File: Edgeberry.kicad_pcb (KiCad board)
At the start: 2 copper layers, 135 x 90 mm, 171 parts, among them J1 Molex_KK_1x02_P2.54mm_CONN, P1 Barrel_Jack_CONN, Q1 BC547, Q2 BC547, Q3 BC547, SW1 SW_PUSH, U1 24LC256, U2 LM2596S-5.0

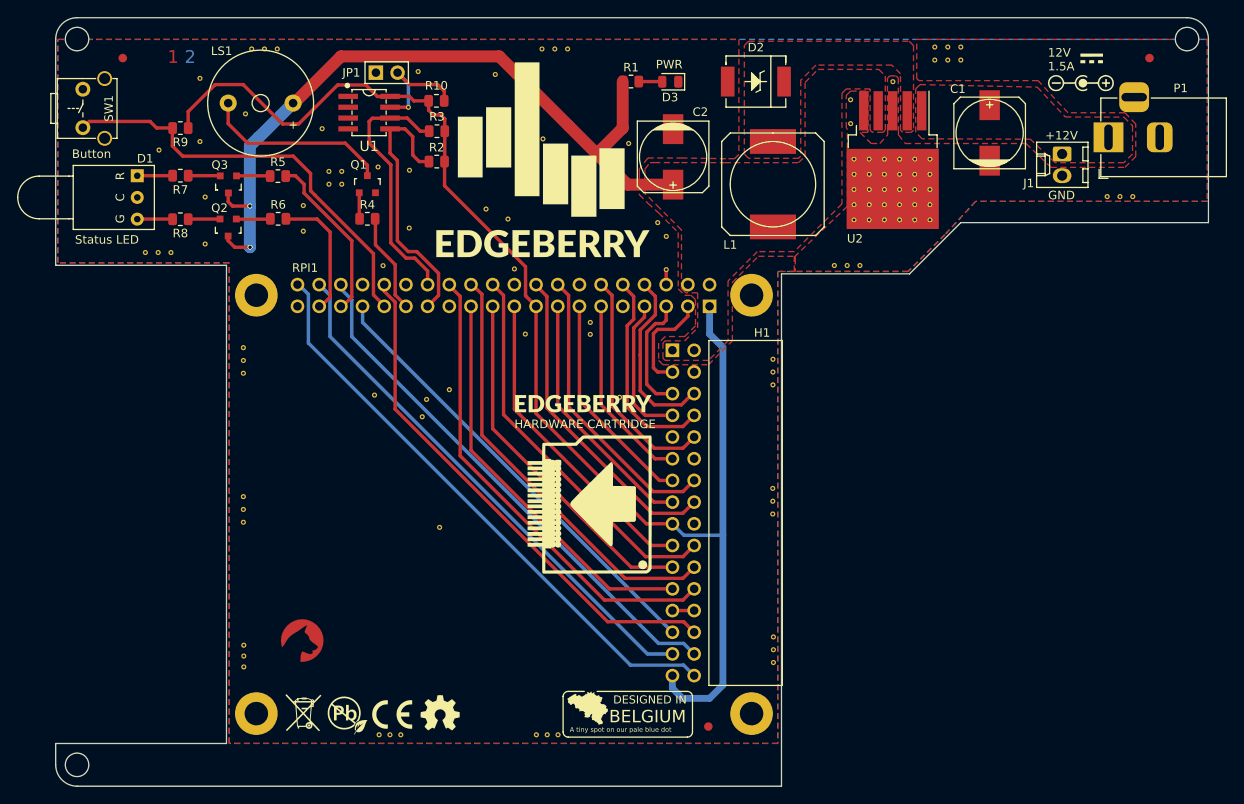
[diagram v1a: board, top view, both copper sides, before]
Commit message: Board:  improvements for fabrications
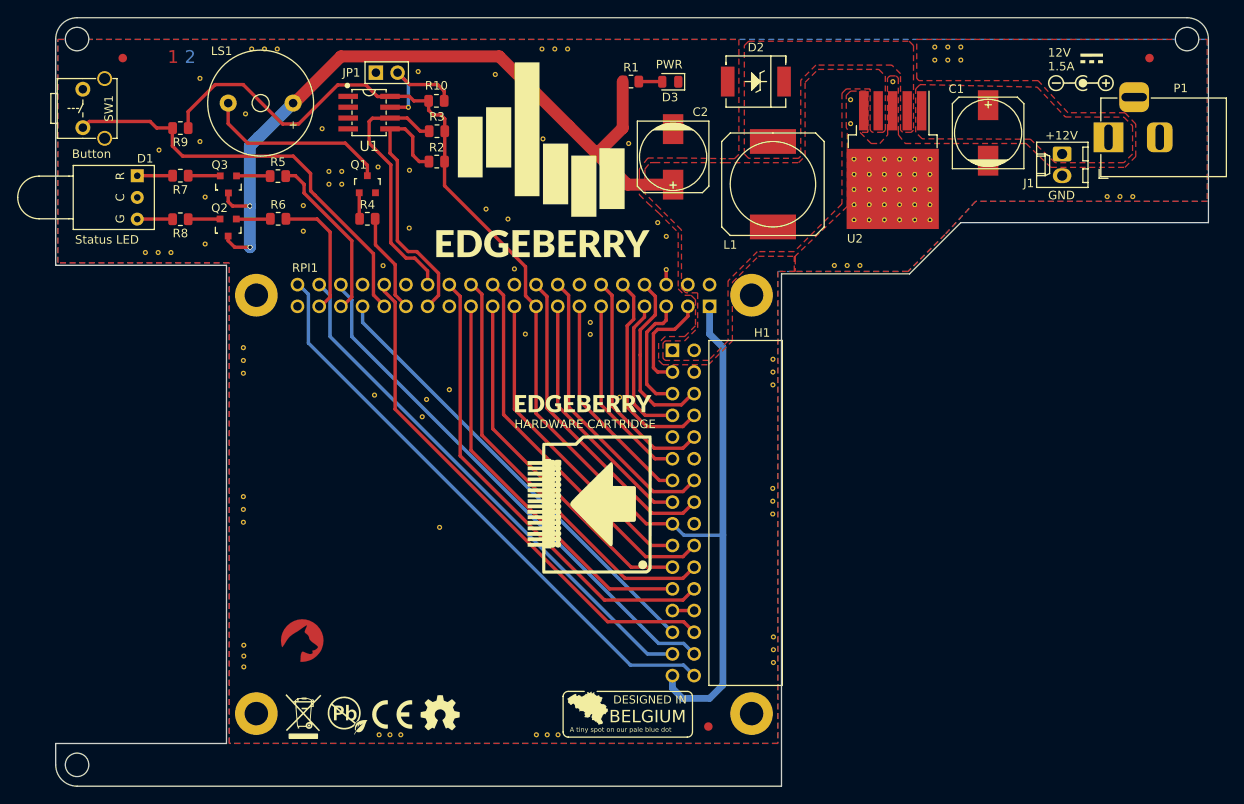
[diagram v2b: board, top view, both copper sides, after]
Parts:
- H1: value 2X16Pin_2.54mm_Right_Angle_Receptacle_Connector -> 2X16Pin_P2.54mm_Horizontal_Receptacle_Connector
- RPI1: value 2X20Pin_2.54mm_Receptacle_Connector -> 2X20Pin_2.54mm_Receptacle_CONN
- SW1: value SW_PUSH -> SW_PUSH_Horizontal
- moved C1 0.18 mm to (192.8, 65.3)
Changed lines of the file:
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@@
   (net 43 "Net-(Q3-Pad2)")
   (footprint "Capacitors_SMD:c_elec_8x10" (layer "F.Cu")
-    (at 193.028 65.2672 90)
+    (at 192.849 65.2672 90)
     (descr "SMT capacitor, aluminium electrolytic, 8x10")
     (property "Sheetfile" "Edgeberry.kicad_sch")
@@
       (effects (font (size 1 1) (thickness 0.15)))
     )
-    (fp_text value "SW_PUSH" (at 0 1.905 -90) (layer "F.Fab")
+    (fp_text value "SW_PUSH_Horizontal" (at -5.076 -4.72) (layer "F.Fab")
       (effects (font (size 1 1) (thickness 0.15)))
     )
@@
       (effects (font (size 1 1) (thickness 0.15)))
     )
-    (fp_text value "SS54" (at -0.2054 2.3342) (layer "F.Fab")
+    (fp_text value "SS54" (at -0.35 2.172) (layer "F.Fab")
       (effects (font (size 1 1) (thickness 0.15)))
     )
@@
       (effects (font (size 1 1) (thickness 0.15)))
     )
-    (fp_text value "Buzzer" (at 0 0 180) (layer "F.Fab")
+    (fp_text value "Buzzer" (at 0 2 180) (layer "F.Fab")
       (effects (font (size 1 1) (thickness 0.15)))
     )
@@
       (effects (font (size 1 1) (thickness 0.15)))
     )
-    (fp_text value "2X16Pin_2.54mm_Right_Angle_Receptacle_Connector" (at 0 -4.85 -90) (layer "F.Fab")
+    (fp_text value "2X16Pin_P2.54mm_Horizontal_Receptacle_Connector" (at 0 -4.85 -90) (layer "F.Fab")
       (effects (font (size 1 1) (thickness 0.15)))
     )
@@
       (effects (font (size 1 1) (thickness 0.15)))
     )
-    (fp_text value "10k" (at 2.937 0) (layer "F.Fab")
+    (fp_text value "10k" (at 2.575 0.048) (layer "F.Fab")
       (effects (font (size 1 1) (thickness 0.15)))
     )
@@
       (effects (font (size 1 1) (thickness 0.15)))
     )
-    (fp_text value "LM2596S-5.0" (at 0.681 6.4514 90) (layer "F.Fab")
+    (fp_text value "LM2596S-5.0" (at 2.175 5.975 90) (layer "F.Fab")
       (effects (font (size 1 1) (thickness 0.15)))
     )
@@
       (effects (font (size 1 1) (thickness 0.15)))
     )
-    (fp_text value "10k" (at -3.048 0) (layer "F.Fab")
+    (fp_text value "10k" (at -2.5355 -0.086) (layer "F.Fab")
       (effects (font (size 1 1) (thickness 0.15)))
     )
@@
       (effects (font (size 1 1) (thickness 0.15)))
     )
-    (fp_text value "10k" (at 2.962 0) (layer "F.Fab")
+    (fp_text value "10k" (at 2.6 0.042) (layer "F.Fab")
       (effects (font (size 1 1) (thickness 0.15)))
     )
@@
       (effects (font (size 1 1) (thickness 0.15)))
     )
-    (fp_text value "2X20Pin_2.54mm_Receptacle_Connector" (at -1.9546 -3.1495 180) (layer "F.Fab")
+    (fp_text value "2X20Pin_2.54mm_Receptacle_CONN" (at -1.9546 -3.1495 180) (layer "F.Fab")
       (effects (font (size 1 1) (thickness 0.15)))
     )
@@
   (gr_line (start 143.073264 131.247736) (end 143.073264 135.423472) (layer "F.SilkS") (width 0.15))
   (gr_arc (start 143.673264 136.023472) (mid 143.249 135.847736) (end 143.073264 135.423472) (layer "F.SilkS") (width 0.15))
+  (gr_poly
+    (pts
+      (xy 114.299 136.172)
+      (xy 110.999 136.172)
+      (xy 110.999 135.672)
+      (xy 114.299 135.672)
+    ) (layer "F.SilkS") (width 0.15) (fill solid))
   (gr_line (start 145.549 130.672) (end 143.673264 130.672) (layer "F.SilkS") (width 0.15))
   (gr_arc (start 158.224736 135.423472) (mid 158.049 135.847736) (end 157.624736 136.023472) (layer "F.SilkS") (width 0.15))
@@
   (gr_line (start 135.6464 84.271) (end 136.6464 84.271) (layer "Margin") (width 0.2))
   (gr_line (start 136.1464 83.771) (end 136.1464 84.771) (layer "Margin") (width 0.2))
+  (gr_line (start 110.799 84.472) (end 110.799 86.672) (layer "F.Fab") (width 0.1))
+  (gr_line (start 154.124 128.522) (end 154.124 129.272) (layer "F.Fab") (width 0.1))
+  (gr_line (start 110.149 86.022) (end 110.799 85.572) (layer "F.Fab") (width 0.1))
+  (gr_line (start 154.124 129.272) (end 154.774 128.822) (layer "F.Fab") (width 0.1))
+  (gr_line (start 154.774 128.822) (end 154.124 128.522) (layer "F.Fab") (width 0.1))
+  (gr_line (start 154.774 127.722) (end 154.774 129.922) (layer "F.Fab") (width 0.1))
+  (gr_line (start 154.774 129.922) (end 157.024 129.922) (layer "F.Fab") (width 0.1))
+  (gr_line (start 110.799 85.572) (end 110.149 85.272) (layer "F.Fab") (width 0.1))
+  (gr_line (start 157.024 129.922) (end 157.024 127.722) (layer "F.Fab") (width 0.1))
+  (gr_line (start 113.049 84.472) (end 110.799 84.472) (layer "F.Fab") (width 0.1))
+  (gr_line (start 113.049 86.672) (end 113.049 84.472) (layer "F.Fab") (width 0.1))
+  (gr_line (start 110.149 85.272) (end 110.149 86.022) (layer "F.Fab") (width 0.1))
+  (gr_line (start 110.799 86.672) (end 113.049 86.672) (layer "F.Fab") (width 0.1))
+  (gr_line (start 157.024 127.722) (end 154.774 127.722) (layer "F.Fab") (width 0.1))
   (gr_text "1" (at 97.399 56.372) (layer "F.Cu")
     (effects (font (size 1.5 1.5) (thickness 0.3)))
@@
     (effects (font (size 0.55 0.55) (thickness 0.125)) (justify left))
   )
-  (gr_text "Raspberry Pi" (at 115.999 87.472) (layer "Dwgs.User")
-    (effects (font (size 1 1) (thickness 0.15)))
-  )
-  (gr_text "Edgeberry Hardware" (at 178.5 171.25) (layer "Dwgs.User")
+  (gr_text "Edgeberry Hardware" (at 71.949 25.772) (layer "Dwgs.User")
     (effects (font (size 5 5) (thickness 1)) (justify left))
   )
-  (gr_text "REV.: 1.4, Mid 2024" (at 179 178.75) (layer "Dwgs.User")
+  (gr_text "Raspberry Pi" (at 115.999 87.622) (layer "Dwgs.User")
+    (effects (font (size 1 1) (thickness 0.15)))
+  )
+  (gr_text "REV.: 1.4, Mid 2024" (at 72.449 33.272) (layer "Dwgs.User")
     (effects (font (size 2 2) (thickness 0.3)) (justify left))
   )
@@
   (dimension (type aligned) (layer "Dwgs.User")
     (pts (xy 216.149 54.272) (xy 86.149 54.272))
-    (height 10.5)
-    (gr_text "130.0 mm" (at 151.149 41.972) (layer "Dwgs.User")
+    (height 6.8)
+    (gr_text "130,0 mm" (at 151.149 45.672) (layer "Dwgs.User")
       (effects (font (size 1.5 1.5) (thickness 0.3)))
     )
@@
   (dimension (type aligned) (layer "Dwgs.User")
     (pts (xy 218.649 54.272) (xy 83.649 54.272))
-    (height 15)
-    (gr_text "135.0 mm" (at 151.149 37.472) (layer "Dwgs.User")
+    (height 11.5)
+    (gr_text "135,0 mm" (at 151.149 40.972) (layer "Dwgs.User")
       (effects (font (size 1.5 1.5) (thickness 0.3)))
     )
